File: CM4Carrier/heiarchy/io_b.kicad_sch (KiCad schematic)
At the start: 3 parts

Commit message: Additions
- Fixed gitignore (Backups)
- Work on buttons
- Work on ADC for JOYSTICK
- Work on some other stuff
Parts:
- removed J?: Micro_SD_Card, symbol Connector:Micro_SD_Card
- removed Module1: ComputeModule4-CM4, CM4IO:Raspberry-Pi-4-Compute-Module, symbol CM4IO:ComputeModule4-CM4
- removed R?: 10M, symbol Device:R
- added J?: (no value), symbol Connector:USB_A
- added J?: (no value), symbol Connector:USB_C_Receptacle_USB2.0
- added Module?: (no value), symbol CM4IO:ComputeModule4-CM4
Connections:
- net GND: now also J?.4 (GND), J?.5 (Shield), J?.A1 (GND), J?.A12 (GND), J?.B1 (GND), J?.B12 (GND)
- net _5v: now also J?.1 (VBUS)
- new net CC1: J?.A5 (CC1)
- new net CC2: J?.B5 (CC2)
- new net CHARGER_D+: J?.A6 (D+), J?.B6 (D+)
- new net CHARGER_D-: J?.A7 (D-), J?.B7 (D-)
- new net D+: J?.3 (D+), Module?.105 (USB2_P)
- new net D-: J?.2 (D-), Module?.103 (USB2_N)
- new net VBUS_CHARGER: J?.A4 (VBUS), J?.A9 (VBUS), J?.B4 (VBUS), J?.B9 (VBUS)
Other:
- note added: "Do not ground shield on DFP."
- note added: "USB C CHARGING"
- note added: "USB-C DFP"
- note added: "Unused."

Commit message: wiring some stuff
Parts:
- added C?: (no value), symbol Device:C
- added J?: (no value), symbol CM4IO:1-1734248-5
- J?: value (none) -> USB_A
- J?: value (none) -> USB_C_Receptacle_USB2.0
- Module?: value (none) -> ComputeModule4-CM4; footprint (none) -> CM4IO:Raspberry-Pi-4-Compute-Module
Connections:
- net GND: now also Module?.107 (GND), Module?.108 (GND), Module?.113 (GND), Module?.114 (GND), Module?.119 (GND), Module?.120 (GND), Module?.125 (GND), Module?.126 (GND), Module?.131 (GND), Module?.132 (GND), Module?.137 (GND), Module?.138 (GND), Module?.144 (GND), Module?.150 (GND), Module?.155 (GND), Module?.156 (GND), Module?.161 (GND), Module?.162 (GND), Module?.167 (GND), Module?.168 (GND), Module?.173 (GND), Module?.174 (GND), Module?.179 (GND), Module?.180 (GND), Module?.185 (GND), Module?.186 (GND), Module?.191 (GND), Module?.192 (GND), Module?.197 (GND), Module?.198 (GND), C?.2, J?.1, J?.10, J?.13, J?.4, J?.7
- net DSI0_L0_DN1: now reaches Module?.157 (DSI0_D0_N)
- net DSI0_L0_DP1: now reaches Module?.159 (DSI0_D0_P)
- net DSI0_L1_DN1: now reaches Module?.163 (DSI0_D1_N)
- net DSI0_L1_DP1: now reaches Module?.165 (DSI0_D1_P)
- net DSI0_CN: now reaches Module?.169 (DSI0_C_N)
- net DSI0_CP: now reaches Module?.171 (DSI0_C_P)
- new net DSI0_DN1: J?.8
- new net DSI0_DP1: J?.9
- new net DSI1_CN: J?.5
- new net DSI1_CP: J?.6
- new net DSI1_DN1: J?.2
- new net DSI1_DP1: J?.3
- new net _3.3v: C?.1, J?.14, J?.15
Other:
- note added: "DSI CONNECTOR (SCREEN)"
- note added: "USB A (2.0)"
- moved on the sheet: J?, Module?B

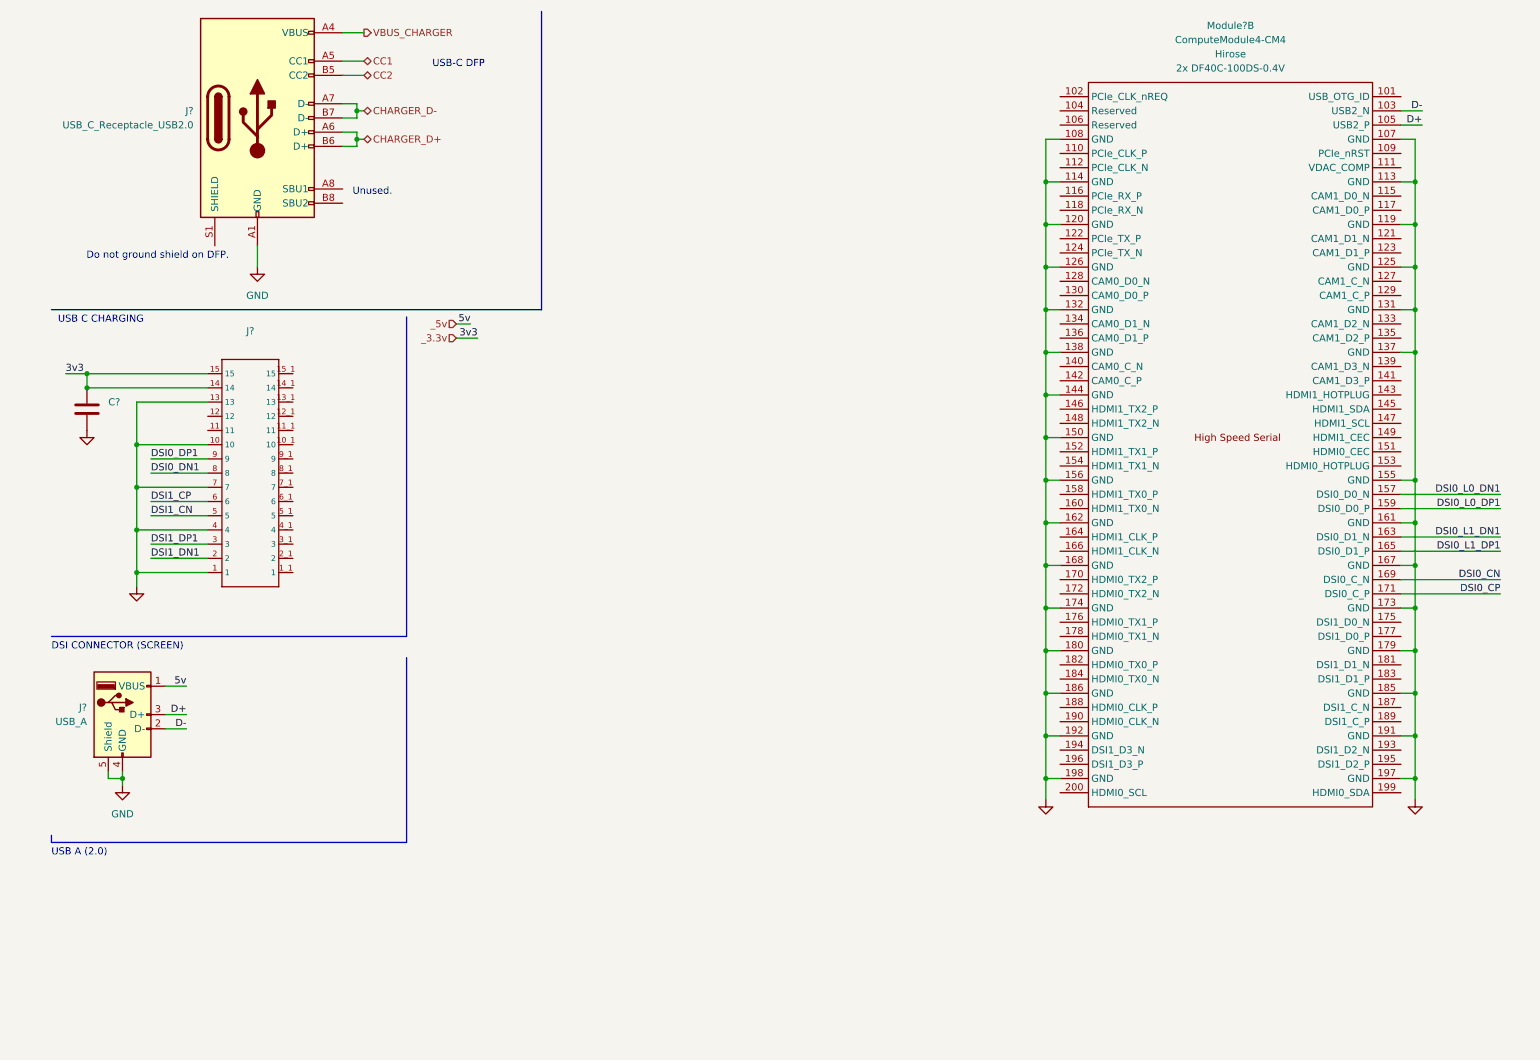
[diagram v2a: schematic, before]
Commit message: footprints  + values
need to do some 3d babeeeeeeeeee
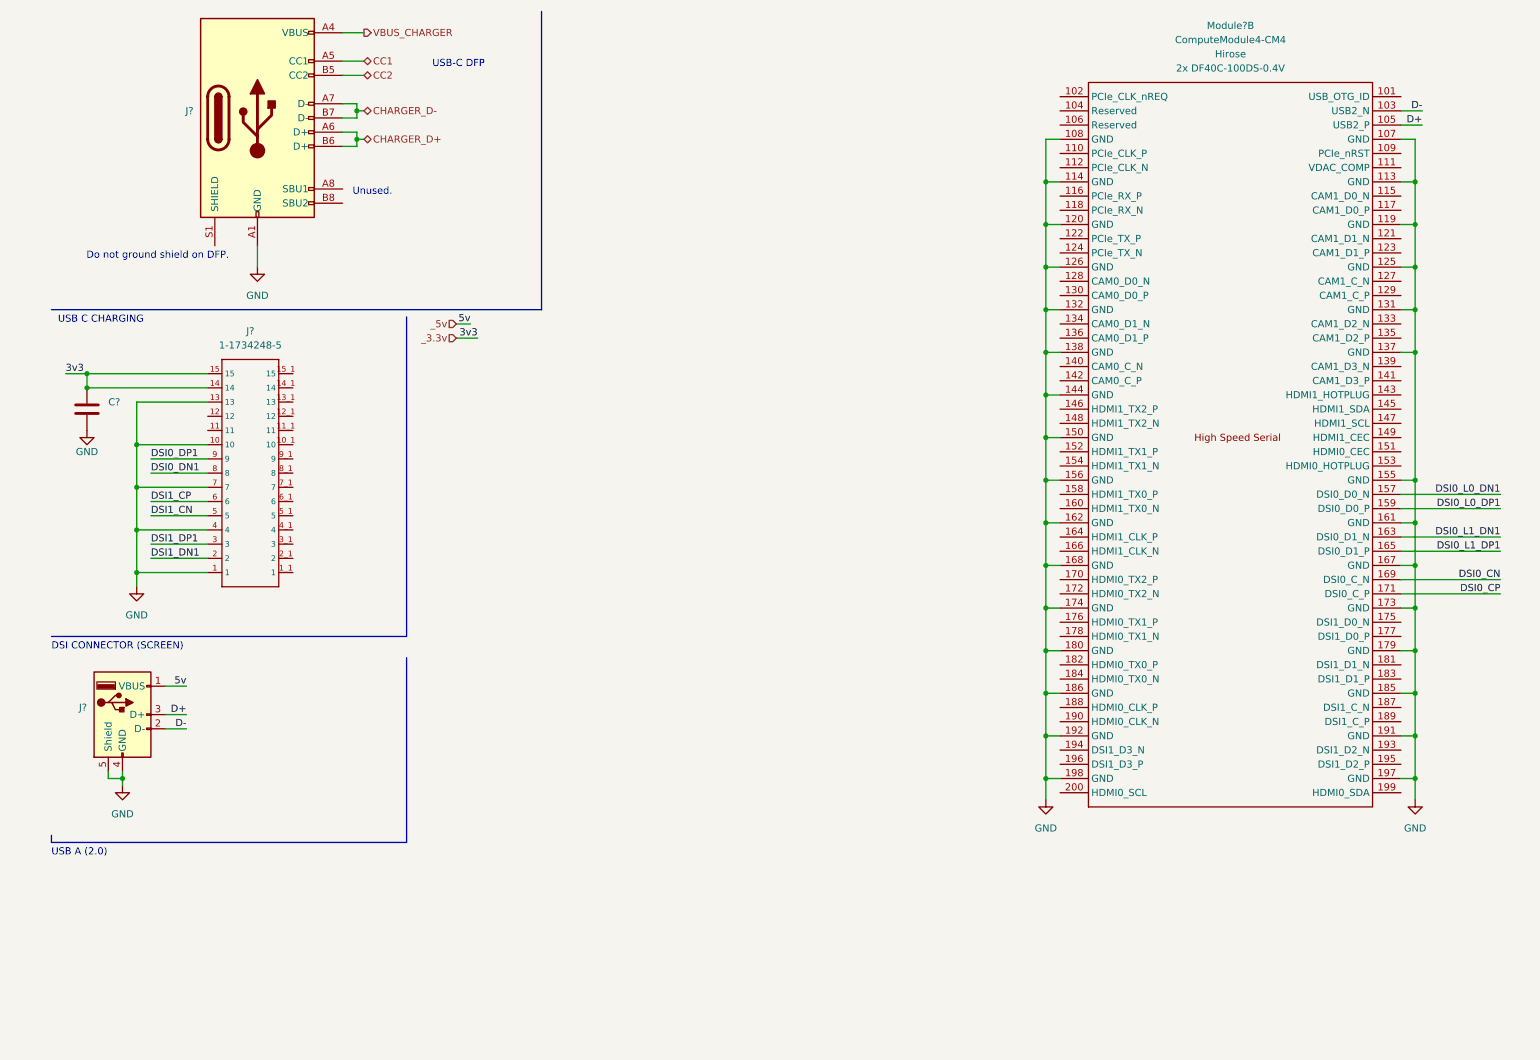
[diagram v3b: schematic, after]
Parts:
- J?: value USB_A -> (none)
- J?: value USB_C_Receptacle_USB2.0 -> (none)
- J?: value (none) -> 1-1734248-5; footprint (none) -> TE_1-1734248-5
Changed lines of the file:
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@@
       (effects (font (size 1.27 1.27)) hide)
     )
-    (property "Value" "" (id 1) (at 20.32 91.44 0))
+    (property "Value" "GND" (id 1) (at 20.32 91.44 0))
     (property "Footprint" "" (id 2) (at 20.32 87.63 0)
       (effects (font (size 1.27 1.27)) hide)
@@
       (effects (font (size 1.27 1.27)) (justify right))
     )
-    (property "Value" "USB_A" (id 1) (at 20.32 139.6999 0)
+    (property "Value" "" (id 1) (at 20.32 139.6999 0)
       (effects (font (size 1.27 1.27)) (justify right))
     )
@@
       (effects (font (size 1.27 1.27)) hide)
     )
-    (property "Value" "" (id 1) (at 257.81 158.75 0))
+    (property "Value" "GND" (id 1) (at 257.81 158.75 0))
     (property "Footprint" "" (id 2) (at 257.81 153.67 0)
       (effects (font (size 1.27 1.27)) hide)
@@
       (effects (font (size 1.27 1.27)) hide)
     )
-    (property "Value" "" (id 1) (at 191.77 158.75 0))
+    (property "Value" "GND" (id 1) (at 191.77 158.75 0))
     (property "Footprint" "" (id 2) (at 191.77 153.67 0)
       (effects (font (size 1.27 1.27)) hide)
@@
       (effects (font (size 1.27 1.27)) (justify right))
     )
-    (property "Value" "USB_C_Receptacle_USB2.0" (id 1) (at 39.37 33.0199 0)
+    (property "Value" "" (id 1) (at 39.37 33.0199 0)
       (effects (font (size 1.27 1.27)) (justify right))
     )
-    (property "Footprint" "" (id 2) (at 54.61 31.75 0)
-      (effects (font (size 1.27 1.27)) hide)
-    )
-    (property "Datasheet" "https://www.usb.org/sites/default/files/documents/usb_type-c.zip" (id 3) (at 54.61 31.75 0)
+    (property "Footprint" "" (id 2) (at 54.61 31.75 0))
+    (property "Datasheet" "https://www.mouser.co.uk/datasheet/2/837/USB4110-2888203.pdf" (id 3) (at 54.61 31.75 0)
       (effects (font (size 1.27 1.27)) hide)
     )
@@
       (effects (font (size 1.27 1.27)) hide)
     )
-    (property "Value" "" (id 1) (at 29.21 120.65 0))
+    (property "Value" "GND" (id 1) (at 29.21 120.65 0))
     (property "Footprint" "" (id 2) (at 29.21 115.57 0)
       (effects (font (size 1.27 1.27)) hide)
@@
     (in_bom yes) (on_board yes) (fields_autoplaced)
     (property "Reference" "J?" (id 0) (at 49.53 69.85 0))
-    (property "Value" "" (id 1) (at 49.53 72.39 0))
-    (property "Footprint" "" (id 2) (at 49.53 95.25 0)
+    (property "Value" "1-1734248-5" (id 1) (at 49.53 72.39 0))
+    (property "Footprint" "TE_1-1734248-5" (id 2) (at 49.53 95.25 0)
       (effects (font (size 1.27 1.27)) (justify left bottom) hide)
     )

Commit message: aa
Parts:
- C?: value (none) -> 100n; footprint (none) -> Capacitor_SMD:C_0805_2012Metric_Pad1.18x1.45mm_HandSolder
- J?: value (none) -> USB_A; footprint (none) -> CM4IO:GCT_USB1125-GF-B_REVA
- J?: value (none) -> USB_C_Receptacle_USB2.0; footprint (none) -> CM4IO:GCT_USB4110-GF-A_REVB
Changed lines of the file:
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@@
       (effects (font (size 1.27 1.27)) (justify right))
     )
-    (property "Value" "" (id 1) (at 20.32 139.6999 0)
+    (property "Value" "USB_A" (id 1) (at 20.32 139.6999 0)
       (effects (font (size 1.27 1.27)) (justify right))
     )
-    (property "Footprint" "" (id 2) (at 30.48 139.7 0)
+    (property "Footprint" "CM4IO:GCT_USB1125-GF-B_REVA" (id 2) (at 30.48 139.7 0)
       (effects (font (size 1.27 1.27)) hide)
     )
@@
       (effects (font (size 1.27 1.27)) (justify left))
     )
-    (property "Value" "" (id 1) (at 24.13 85.0899 0)
+    (property "Value" "100n" (id 1) (at 24.13 85.0899 0)
       (effects (font (size 1.27 1.27)) (justify left))
     )
-    (property "Footprint" "" (id 2) (at 21.2852 87.63 0)
+    (property "Footprint" "Capacitor_SMD:C_0805_2012Metric_Pad1.18x1.45mm_HandSolder" (id 2) (at 21.2852 87.63 0)
       (effects (font (size 1.27 1.27)) hide)
     )
@@
       (effects (font (size 1.27 1.27)) (justify right))
     )
-    (property "Value" "" (id 1) (at 39.37 33.0199 0)
+    (property "Value" "USB_C_Receptacle_USB2.0" (id 1) (at 39.37 33.0199 0)
       (effects (font (size 1.27 1.27)) (justify right))
     )
-    (property "Footprint" "" (id 2) (at 54.61 31.75 0))
+    (property "Footprint" "CM4IO:GCT_USB4110-GF-A_REVB" (id 2) (at 54.61 31.75 0))
     (property "Datasheet" "https://www.mouser.co.uk/datasheet/2/837/USB4110-2888203.pdf" (id 3) (at 54.61 31.75 0)
       (effects (font (size 1.27 1.27)) hide)

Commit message: pcb next :sunglasses:
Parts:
- gave numbers to parts that had none: 5
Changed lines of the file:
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@@
   (symbol (lib_id "power:GND") (at 20.32 87.63 0) (unit 1)
     (in_bom yes) (on_board yes)
-    (property "Reference" "#PWR?" (id 0) (at 20.32 93.98 0)
+    (property "Reference" "#PWR0138" (id 0) (at 20.32 93.98 0)
       (effects (font (size 1.27 1.27)) hide)
     )
@@
   (symbol (lib_id "Connector:USB_A") (at 26.67 138.43 0) (unit 1)
     (in_bom yes) (on_board yes) (fields_autoplaced)
-    (property "Reference" "J?" (id 0) (at 20.32 137.1599 0)
+    (property "Reference" "J3" (id 0) (at 20.32 137.1599 0)
       (effects (font (size 1.27 1.27)) (justify right))
     )
@@
   (symbol (lib_id "CM4IO:ComputeModule4-CM4") (at 85.09 88.9 0) (unit 2)
     (in_bom yes) (on_board yes) (fields_autoplaced)
-    (property "Reference" "Module?" (id 0) (at 224.79 15.24 0))
+    (property "Reference" "Module1" (id 0) (at 224.79 15.24 0))
     (property "Value" "ComputeModule4-CM4" (id 1) (at 224.79 17.78 0))
     (property "Footprint" "CM4IO:Raspberry-Pi-4-Compute-Module" (id 2) (at 227.33 115.57 0)
@@
   (symbol (lib_id "power:GND") (at 257.81 153.67 0) (unit 1)
     (in_bom yes) (on_board yes) (fields_autoplaced)
-    (property "Reference" "#PWR?" (id 0) (at 257.81 160.02 0)
+    (property "Reference" "#PWR0136" (id 0) (at 257.81 160.02 0)
       (effects (font (size 1.27 1.27)) hide)
     )
@@
   (symbol (lib_id "Device:C") (at 20.32 83.82 0) (unit 1)
     (in_bom yes) (on_board yes) (fields_autoplaced)
-    (property "Reference" "C?" (id 0) (at 24.13 82.5499 0)
+    (property "Reference" "C26" (id 0) (at 24.13 82.5499 0)
       (effects (font (size 1.27 1.27)) (justify left))
     )
@@
   (symbol (lib_id "power:GND") (at 50.8 58.42 0) (mirror y) (unit 1)
     (in_bom yes) (on_board yes) (fields_autoplaced)
-    (property "Reference" "#PWR?" (id 0) (at 50.8 64.77 0)
+    (property "Reference" "#PWR0139" (id 0) (at 50.8 64.77 0)
       (effects (font (size 1.27 1.27)) hide)
     )
@@
   (symbol (lib_id "power:GND") (at 191.77 153.67 0) (unit 1)
     (in_bom yes) (on_board yes) (fields_autoplaced)
-    (property "Reference" "#PWR?" (id 0) (at 191.77 160.02 0)
+    (property "Reference" "#PWR0137" (id 0) (at 191.77 160.02 0)
       (effects (font (size 1.27 1.27)) hide)
     )
@@
   (symbol (lib_id "Connector:USB_C_Receptacle_USB2.0") (at 50.8 31.75 0) (unit 1)
     (in_bom yes) (on_board yes) (fields_autoplaced)
-    (property "Reference" "J?" (id 0) (at 39.37 30.4799 0)
+    (property "Reference" "J5" (id 0) (at 39.37 30.4799 0)
       (effects (font (size 1.27 1.27)) (justify right))
     )
@@
   (symbol (lib_id "power:GND") (at 26.67 151.13 0) (mirror y) (unit 1)
     (in_bom yes) (on_board yes) (fields_autoplaced)
-    (property "Reference" "#PWR?" (id 0) (at 26.67 157.48 0)
+    (property "Reference" "#PWR0141" (id 0) (at 26.67 157.48 0)
       (effects (font (size 1.27 1.27)) hide)
     )
@@
   (symbol (lib_id "power:GND") (at 29.21 115.57 0) (unit 1)
     (in_bom yes) (on_board yes) (fields_autoplaced)
-    (property "Reference" "#PWR?" (id 0) (at 29.21 121.92 0)
+    (property "Reference" "#PWR0140" (id 0) (at 29.21 121.92 0)
       (effects (font (size 1.27 1.27)) hide)
     )
@@
   (symbol (lib_id "CM4IO:1-1734248-5") (at 49.53 95.25 0) (mirror x) (unit 1)
     (in_bom yes) (on_board yes) (fields_autoplaced)
-    (property "Reference" "J?" (id 0) (at 49.53 69.85 0))
+    (property "Reference" "J4" (id 0) (at 49.53 69.85 0))
     (property "Value" "1-1734248-5" (id 1) (at 49.53 72.39 0))
     (property "Footprint" "TE_1-1734248-5" (id 2) (at 49.53 95.25 0)

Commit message: pcb babeee les goooo
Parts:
- removed J4: 1-1734248-5, TE_1-1734248-5, symbol CM4IO:1-1734248-5
- added J5: 1-84952-5, CM4IO:TE_1-84952-5, symbol 84952-5:1-84952-5
- added R38: nc, Resistor_SMD:R_0805_2012Metric_Pad1.20x1.40mm_HandSolder, symbol Device:R
- renumbered J5 to J4
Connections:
- net DSI0_CN: now also J5.5
- net DSI0_CP: now also J5.6
- net DSI0_L0_DN1: now also J5.8
- net DSI0_L0_DP1: now also J5.9
- net DSI0_L1_DN1: now also J5.2
- net DSI0_L1_DP1: now also J5.3
- net GND: now also J5.1, J5.10, J5.13, J5.4, J5.7, J5.S1 (SHIELD), J5.S2 (SHIELD), R38.2
- net _3.3v: now also J5.14, J5.15
- net at J4.S1 (SHIELD): now also R38.1
- no-connect marks 0 -> 67
